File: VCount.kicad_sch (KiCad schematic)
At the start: 4 parts, among them U2 GAL22V10, U203 74HC163, U204 74HC163, U205 74HC163

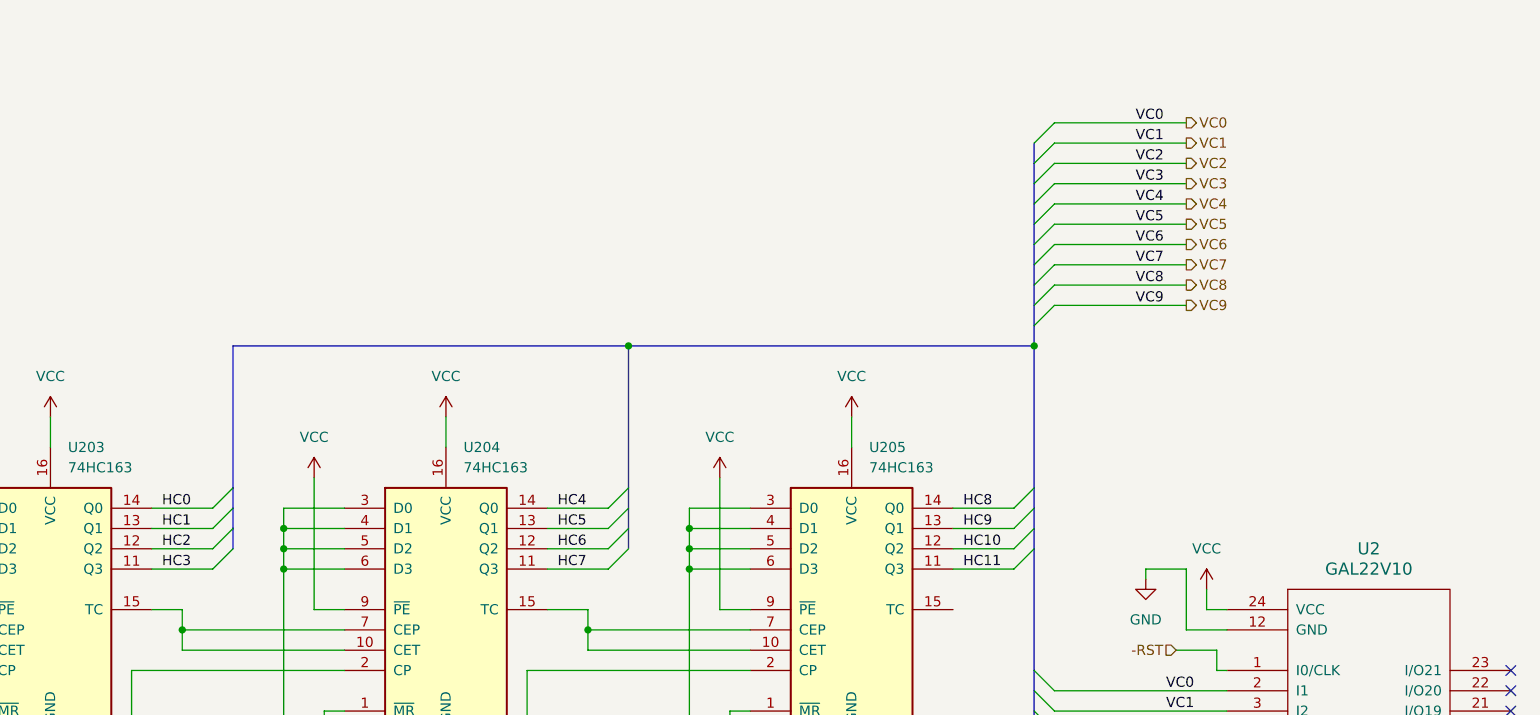
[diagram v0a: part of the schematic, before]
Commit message: add decoupling caps, fix net labels
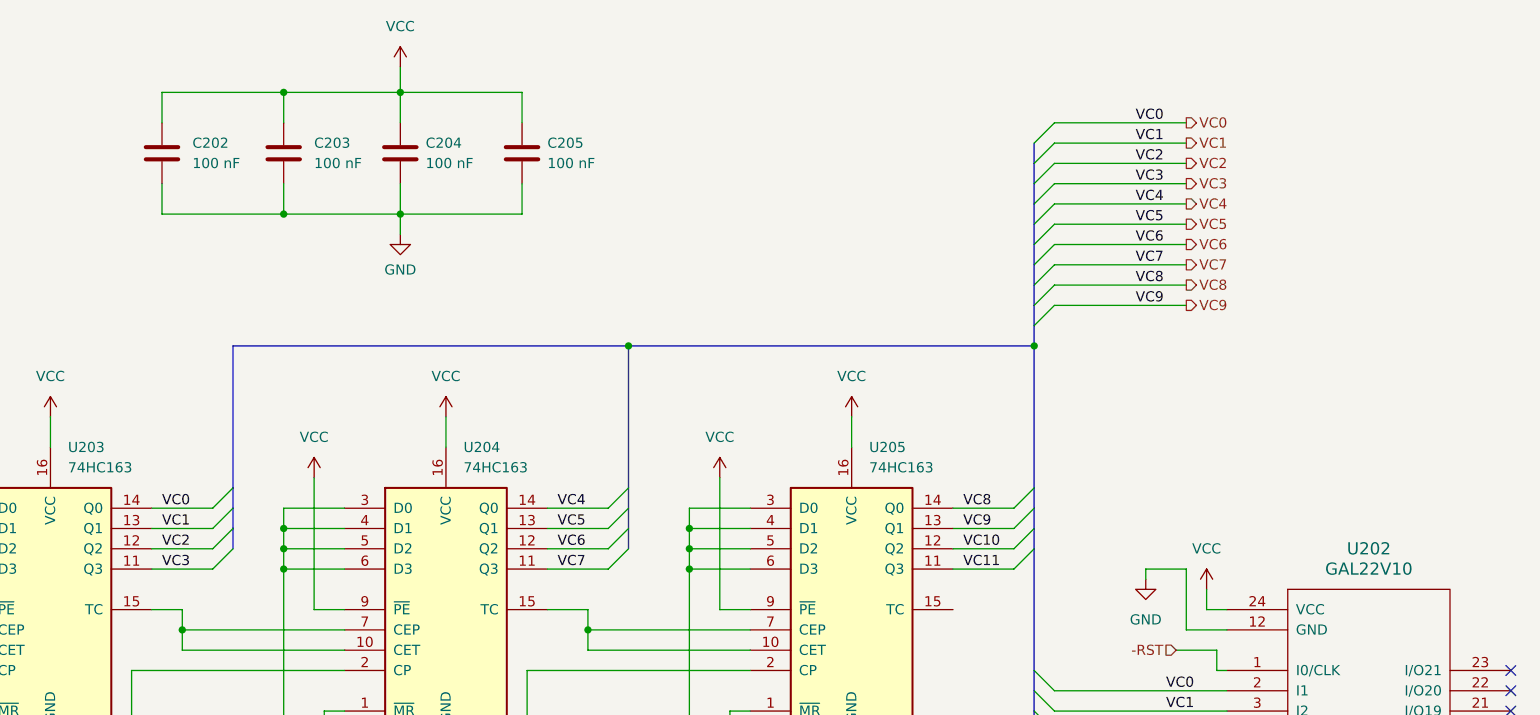
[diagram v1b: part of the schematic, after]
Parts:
- added C202, C203, C204, C205: 100 nF, symbol Device:C
- renumbered U2 to U202
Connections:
- net HC0 is gone; now on net VC0: U203.14 (Q0)
- net HC1 is gone; now on net VC1: U203.13 (Q1)
- net HC2 is gone; now on net VC2: U203.12 (Q2)
- net HC3 is gone; now on net VC3: U203.11 (Q3)
- net HC4 is gone; now on net VC4: U204.14 (Q0)
- net HC5 is gone; now on net VC5: U204.13 (Q1)
- net HC6 is gone; now on net VC6: U204.12 (Q2)
- net HC7 is gone; now on net VC7: U204.11 (Q3)
- net HC8 is gone; now on net VC8: U205.14 (Q0)
- net HC9 is gone; now on net VC9: U205.13 (Q1)
- net GND: now also C202.2, C203.2, C204.2, C205.2
- net VCC: now also C202.1, C203.1, C204.1, C205.1
- net HC10 renamed VC10
- net HC11 renamed VC11

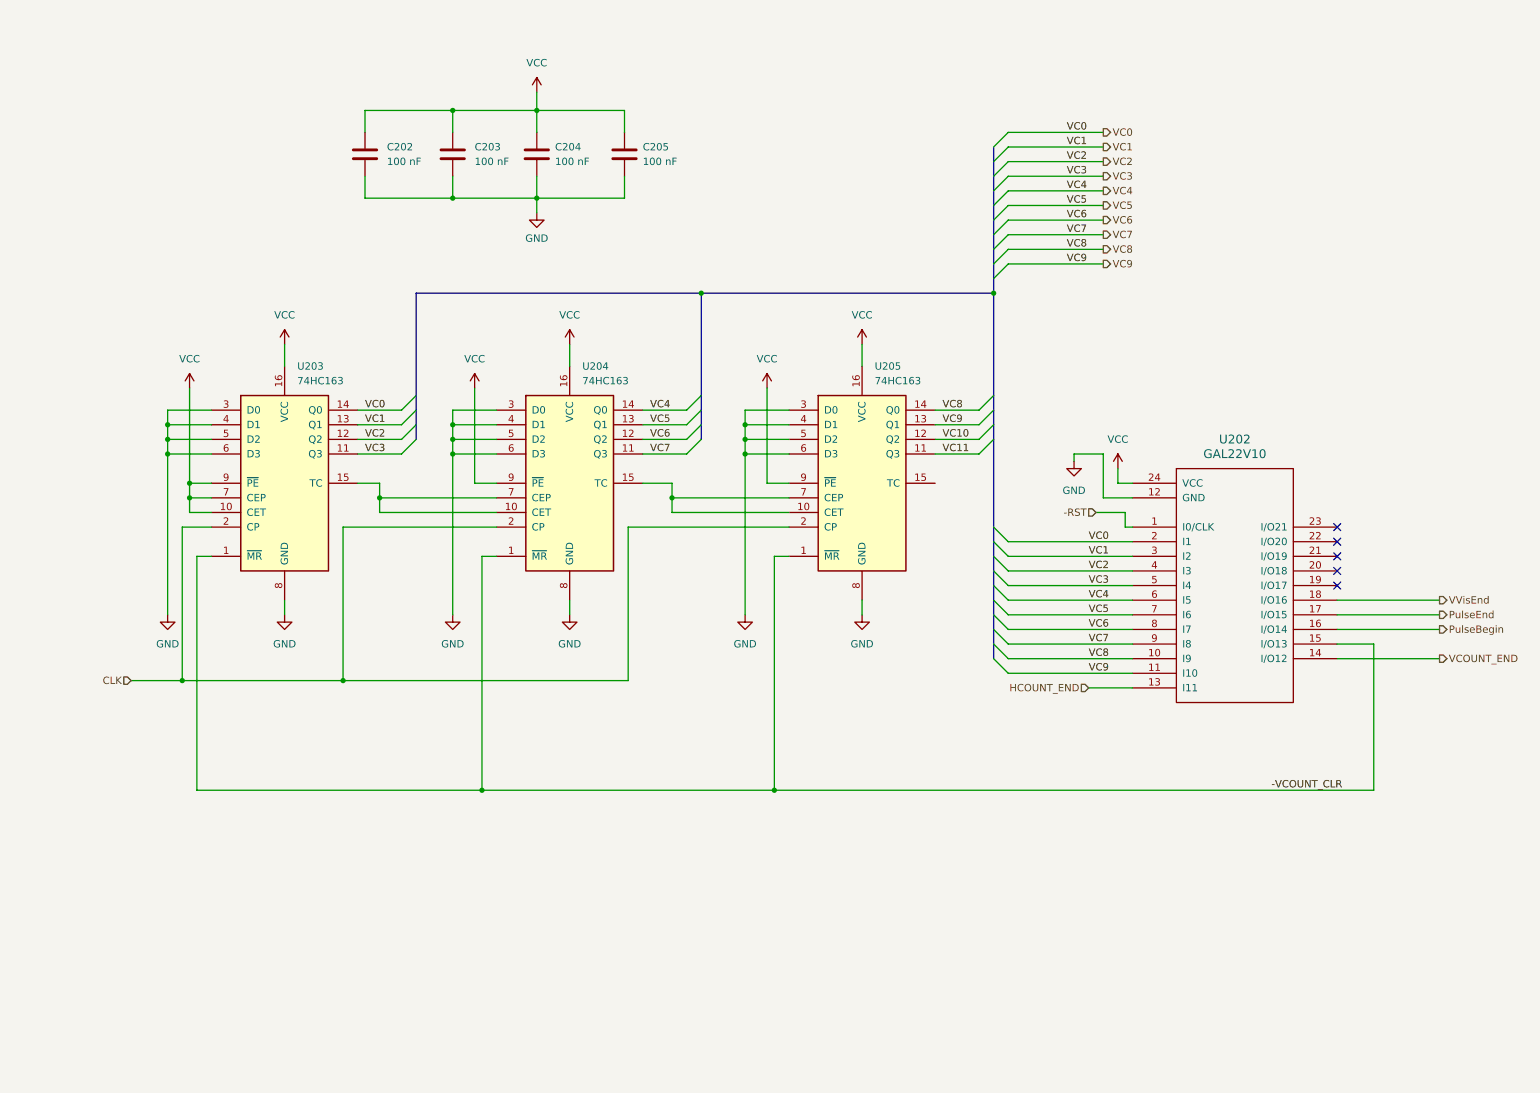
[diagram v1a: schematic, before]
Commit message: set VCOUNT initially in vertical back porch
This means that VVis should *not* be asserted
initially, but should only be asserted once
the first proper frame begins.
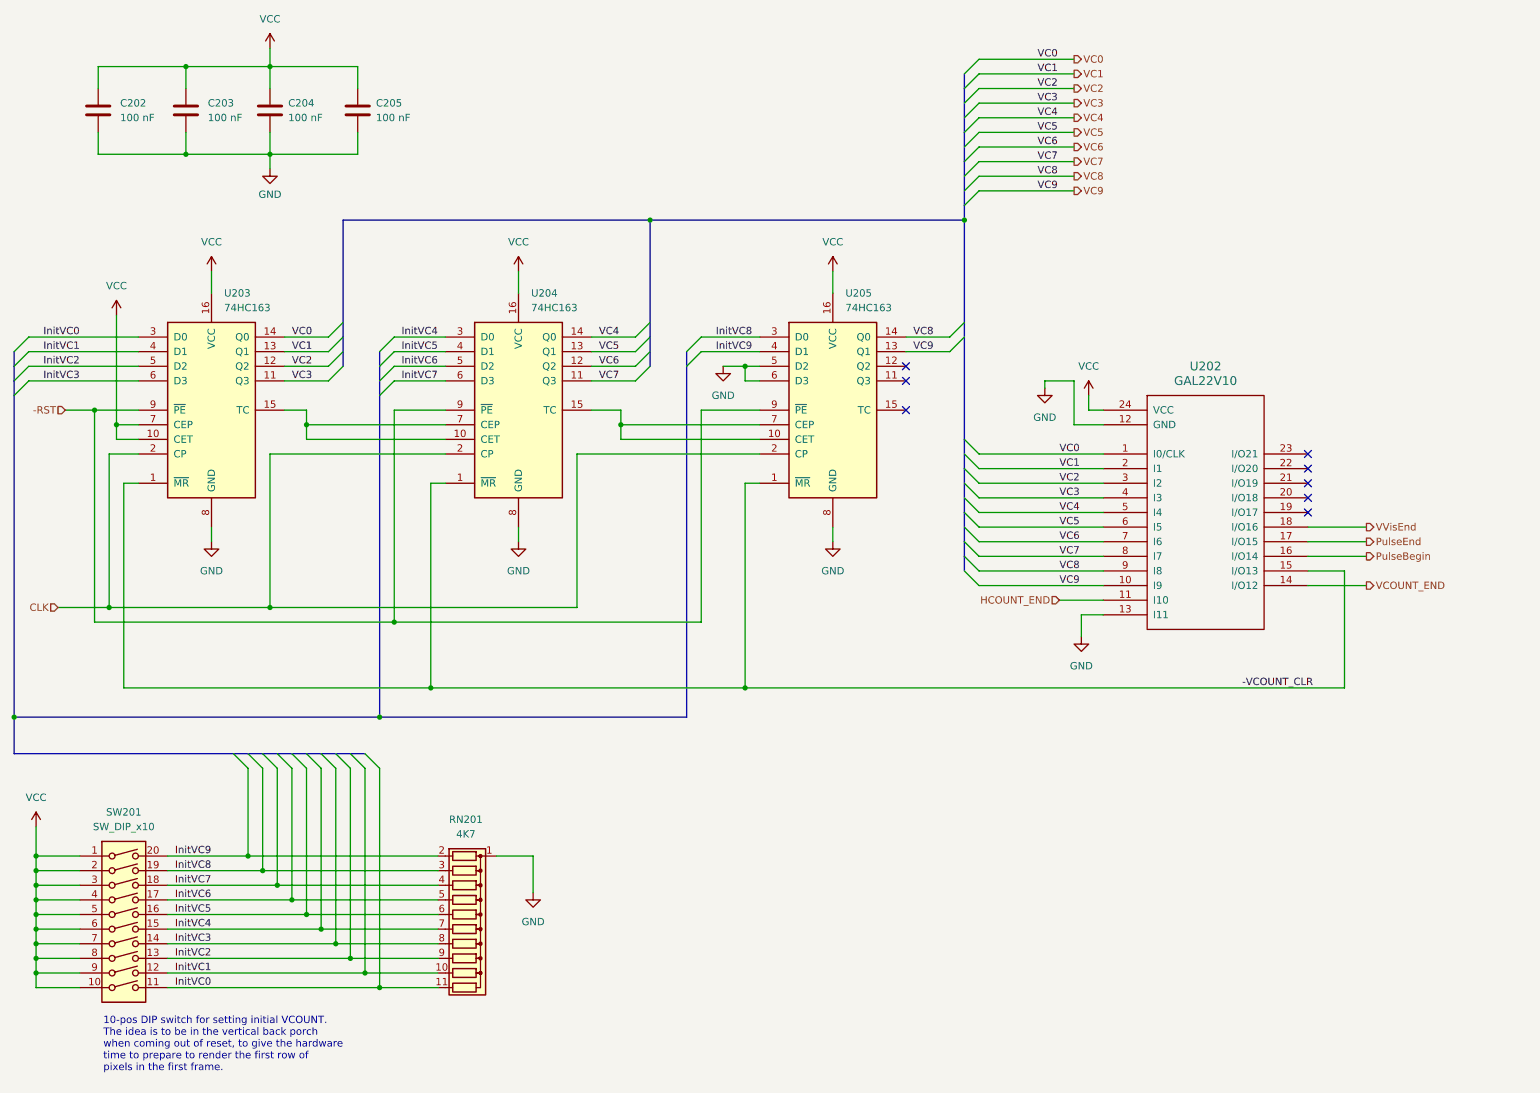
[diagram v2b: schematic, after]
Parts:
- added RN201: 4K7, Resistor_THT:R_Array_SIP11, symbol Device:R_Network10
- added SW201: SW_DIP_x10, symbol Switch:SW_DIP_x10
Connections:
- net -RST: now also U203.9 (~{PE}), U204.9 (~{PE}), U205.9 (~{PE}); no longer U202.1 (I0/CLK)
- net GND: now also U202.13 (I11), RN201.1 (common); no longer U203.3 (D0), U203.4 (D1), U203.5 (D2), U203.6 (D3), U204.3 (D0), U204.4 (D1), U204.5 (D2), U204.6 (D3), U205.3 (D0), U205.4 (D1)
- net HCOUNT_END: now also U202.11 (I10); no longer U202.13 (I11)
- net VC0: now also U202.1 (I0/CLK); no longer U202.2 (I1)
- net VC1: now also U202.2 (I1); no longer U202.3 (I2)
- net VC2: now also U202.3 (I2); no longer U202.4 (I3)
- net VC3: now also U202.4 (I3); no longer U202.5 (I4)
- net VC4: now also U202.5 (I4); no longer U202.6 (I5)
- net VC5: now also U202.6 (I5); no longer U202.7 (I6)
- net VC6: now also U202.7 (I6); no longer U202.8 (I7)
- net VC7: now also U202.8 (I7); no longer U202.9 (I8)
- net VC8: now also U202.9 (I8); no longer U202.10 (I9)
- net VC9: now also U202.10 (I9); no longer U202.11 (I10)
- net VCC: now also SW201.1, SW201.10, SW201.2, SW201.3, SW201.4, SW201.5, SW201.6, SW201.7, SW201.8, SW201.9; no longer U203.9 (~{PE}), U204.9 (~{PE}), U205.9 (~{PE})
- net VC10: no longer names the net of U205.12 (Q2)
- net VC11: no longer names the net of U205.11 (Q3)
- new net InitVC0: RN201.11 (R10), SW201.11, U203.3 (D0)
- new net InitVC1: RN201.10 (R9), SW201.12, U203.4 (D1)
- new net InitVC2: RN201.9 (R8), SW201.13, U203.5 (D2)
- new net InitVC3: RN201.8 (R7), SW201.14, U203.6 (D3)
- new net InitVC4: RN201.7 (R6), SW201.15, U204.3 (D0)
- new net InitVC5: RN201.6 (R5), SW201.16, U204.4 (D1)
- new net InitVC6: RN201.5 (R4), SW201.17, U204.5 (D2)
- new net InitVC7: RN201.4 (R3), SW201.18, U204.6 (D3)
- new net InitVC8: RN201.3 (R2), SW201.19, U205.3 (D0)
- new net InitVC9: RN201.2 (R1), SW201.20, U205.4 (D1)
- no-connect marks 5 -> 8
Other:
- note added: "10-pos DIP switch for setting initial VCOUNT. The idea is to be in the vertical back porch when coming out of reset, to give the hardware time to prepare to render the first row of pixels in the first frame."
- moved on the sheet: C202, C203, C204, C205, U202, U203, U204, U205

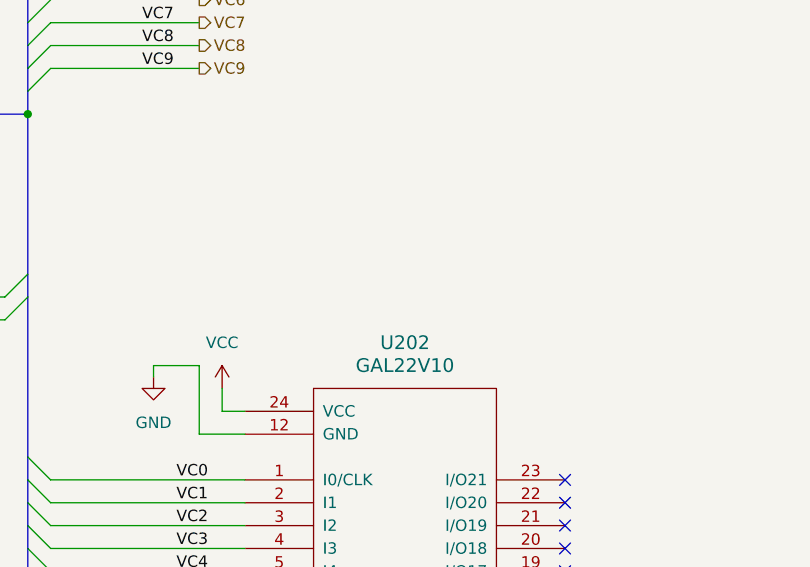
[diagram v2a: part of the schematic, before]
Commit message: use GAL22V10 for Sync module
Also, various improvements/cleanups to schematics.
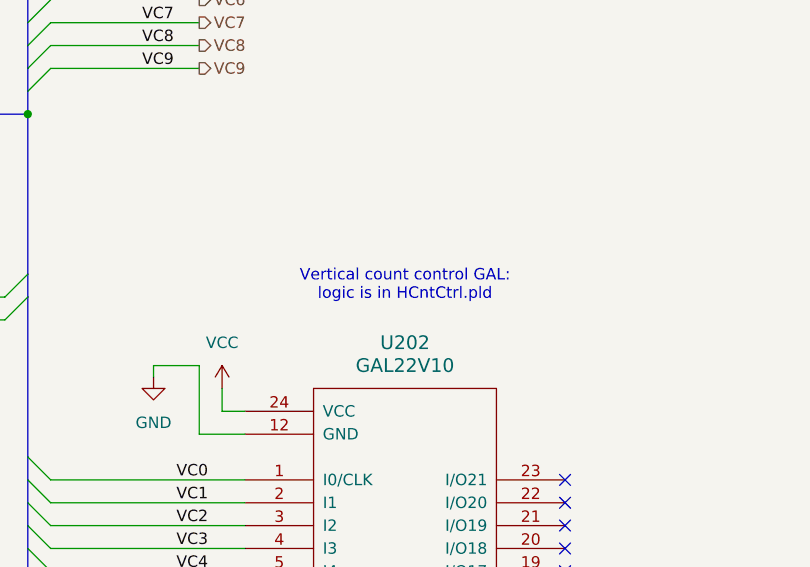
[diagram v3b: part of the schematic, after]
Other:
- note added: "Vertical count control GAL: logic is in HCntCtrl.pld"
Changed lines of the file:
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@@
+		)
+	)
+	(text "Vertical count control GAL:\nlogic is in HCntCtrl.pld"
+		(exclude_from_sim no)
+		(at 220.98 68.58 0)
+		(effects
+			(font
+				(size 1.27 1.27)
+			)
 		)
 	)

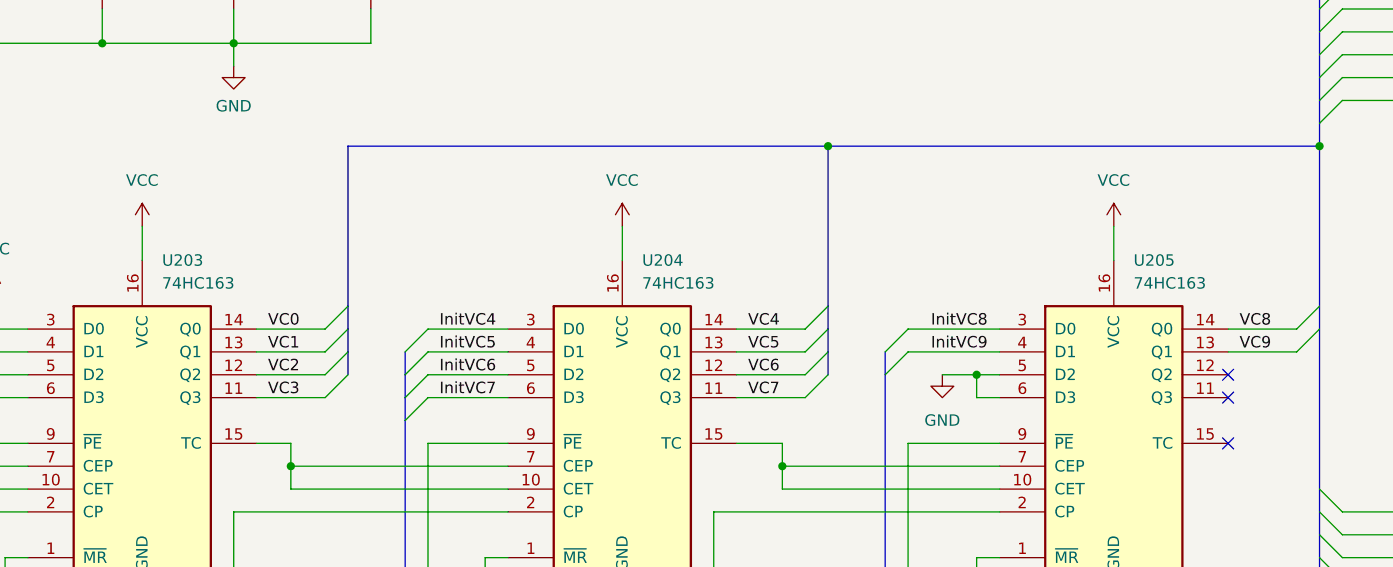
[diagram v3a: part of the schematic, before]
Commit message: chips driven by GAL or memory need to be 74HCT
I forgot that GALs only guarantee 2.4V as the minimum
output high voltage. Bleh.
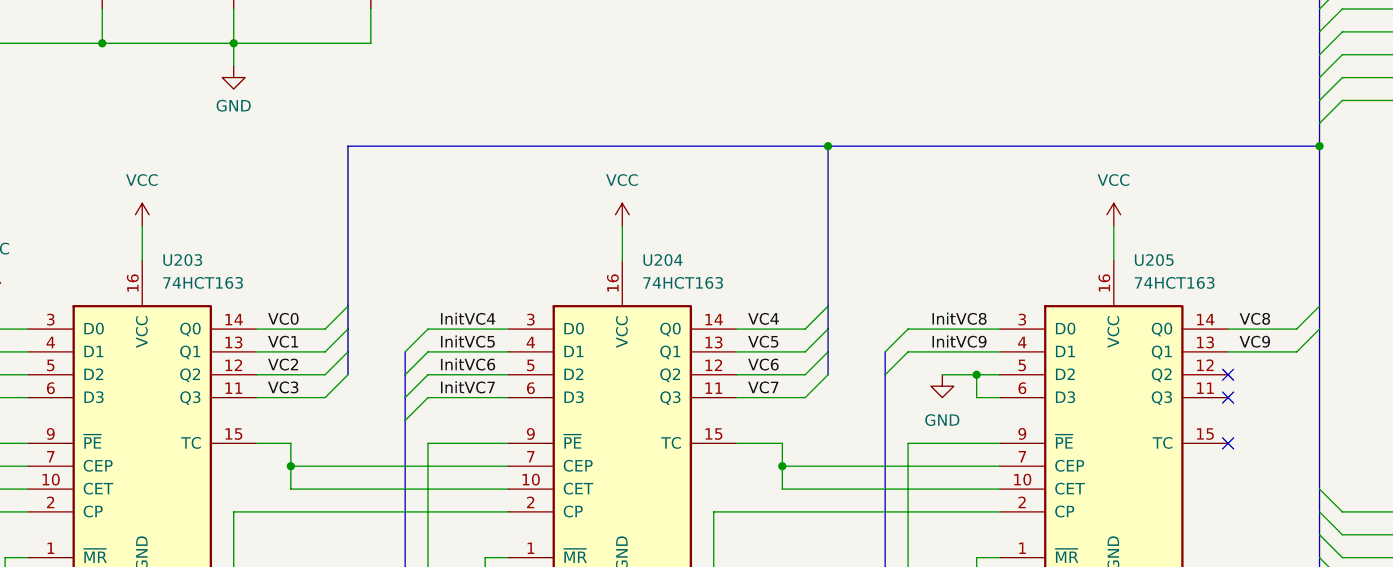
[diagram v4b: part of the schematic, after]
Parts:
- U203, U204, U205: value 74HC163 -> 74HCT163
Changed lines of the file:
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@@
 			)
 		)
-		(property "Value" "74HC163"
+		(property "Value" "74HCT163"
 			(at 158.4041 64.77 0)
 			(effects
@@
 			)
 		)
-		(property "Value" "74HC163"
+		(property "Value" "74HCT163"
 			(at 50.4541 64.77 0)
 			(effects
@@
 			)
 		)
-		(property "Value" "74HC163"
+		(property "Value" "74HCT163"
 			(at 103.7941 64.77 0)
 			(effects
